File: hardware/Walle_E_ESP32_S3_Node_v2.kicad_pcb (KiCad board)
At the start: 2 copper layers, 160 x 100 mm, 50 parts, among them J1 Voltage01_ZMPT101B, J10 Conn_01x22_Pin, J11 Conn_01x22_Pin, J12 Conn_01x08_Pin, J13 Conn_01x08_Pin, J14 Diff_Pressure_Sens LWLP5000, J2 CurrentSens01_ACS712_5A, J4 CurrentSens03_ACS712_5A, J5 Conn_01x04_Pin, J6 +5VdcSupply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

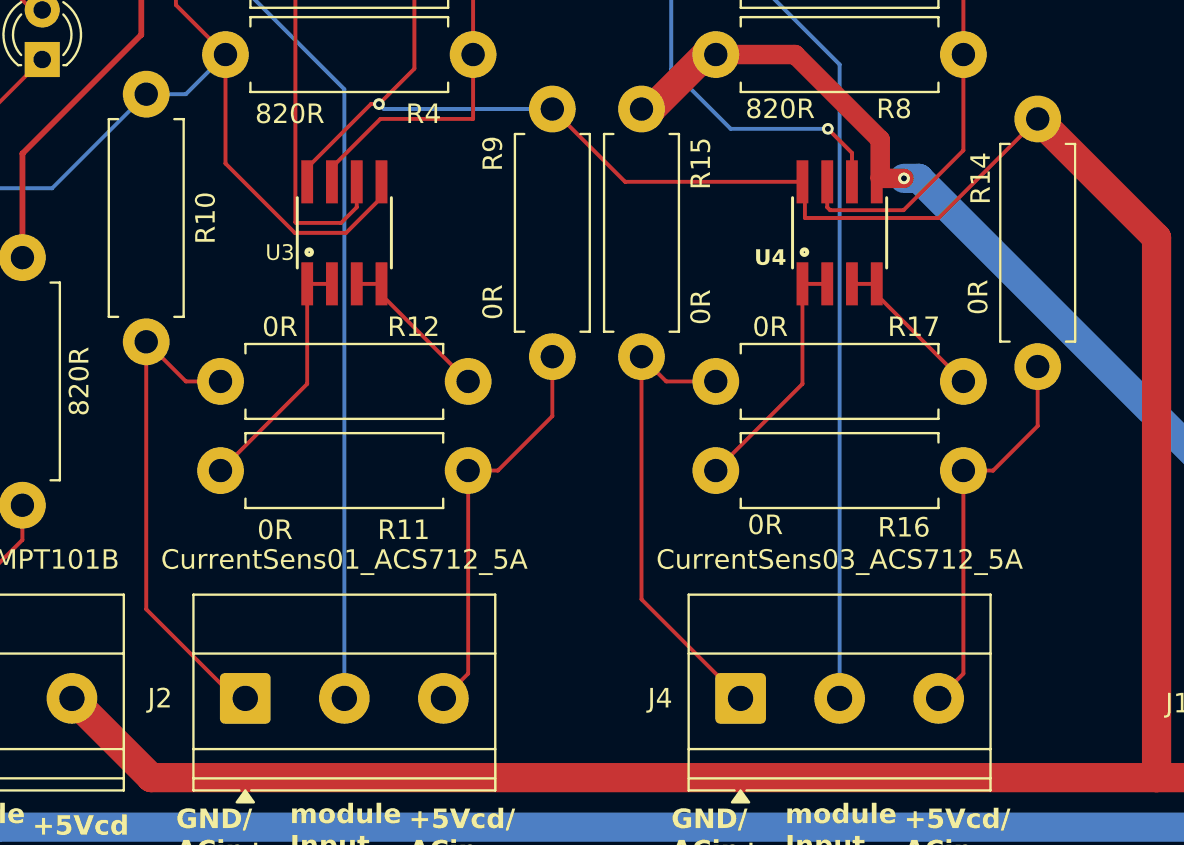
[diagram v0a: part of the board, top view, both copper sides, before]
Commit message: Thickness improve in AC current sensor input AC line
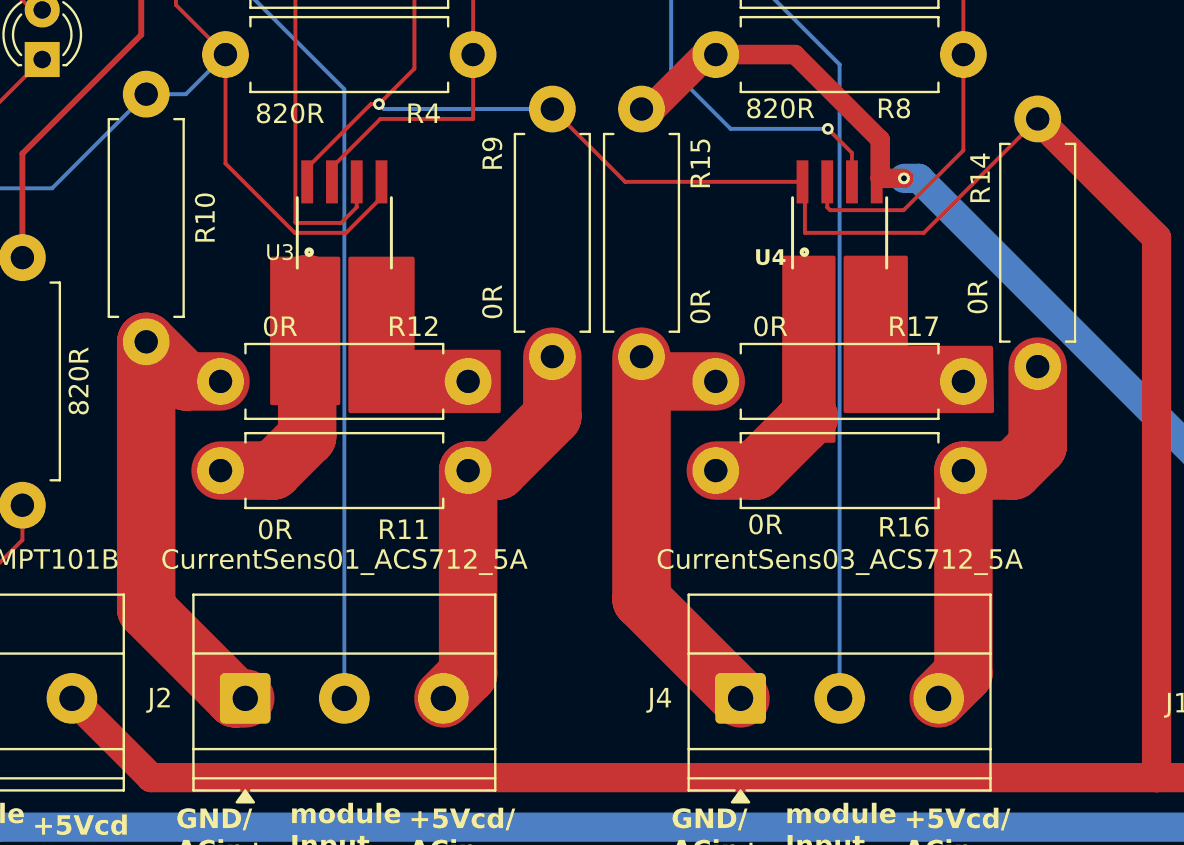
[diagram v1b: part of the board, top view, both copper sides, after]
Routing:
- net Net-(U4-IP-@3): track 8.11 -> 10.3 mm
- net Net-(U3-IP+@1): track 12.7 -> 14.3 mm
- net Net-(U4-IP+@1): track 12.7 -> 11.1 mm
- net +5V_input: track 330.8 -> 331.8 mm
- net Net-(U3-IP-@3): track 8.11 -> 9.14 mm
- net /CurrentSensor01_GND: track 26.1 -> 25.3 mm
- net /CurrentSensor03_+5V: track 20.0 -> 20.6 mm
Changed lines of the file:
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@@
 			(drillshape 0)
 			(scaleselection 1)
-			(outputdirectory "C:/Users/andani.lopez/KiCad projects/Wall_E_ESP32_Node/Wall_E_ESP32_Node_Gerber")
+			(outputdirectory "../Walle_E_ESP32_S3_Node_v2 Gerber/")
 		)
 	)
@@
 		)
 		(embedded_fonts no)
+		(model "${KIPRJMOD}/KiCad libraries/power supply/RAC05-0S5K_277_W/RAC05-05SK_277_W/RAC05-05SK_277_W.step"
+			(offset
+				(xyz 0 0 0)
+			)
+			(scale
+				(xyz 1 1 1)
+			)
+			(rotate
+				(xyz -90 -0 -0)
+			)
+		)
 	)
 	(footprint "TerminalBlock_Phoenix:TerminalBlock_Phoenix_MKDS-3-2-5.08_1x02_P5.08mm_Horizontal"
@@
 		)
 	)
+	(gr_poly
+		(pts
+			(xy 63.2968 68.834) (xy 63.2968 76.708) (xy 70.8152 76.708) (xy 70.7644 73.4568) (xy 66.3956 73.4568)
+			(xy 66.3956 68.834)
+		)
+		(stroke
+			(width 0.2)
+			(type solid)
+		)
+		(fill yes)
+		(layer "F.Cu")
+		(net 63)
+	)
+	(gr_poly
+		(pts
+			(xy 37.8968 68.8848) (xy 37.8968 76.708) (xy 45.5168 76.708) (xy 45.5168 73.66) (xy 41.0972 73.66)
+			(xy 41.0972 68.8848)
+		)
+		(stroke
+			(width 0.2)
+			(type solid)
+		)
+		(fill yes)
+		(layer "F.Cu")
+		(net 61)
+	)
+	(gr_poly
+		(pts
+			(xy 37.2872 76.3016) (xy 33.8836 76.3016) (xy 33.8836 68.8848) (xy 37.2872 68.8848)
+		)
+		(stroke
+			(width 0.2)
+			(type solid)
+		)
+		(fill yes)
+		(layer "F.Cu")
+		(net 60)
+	)
+	(gr_poly
+		(pts
+			(xy 60.1472 68.834) (xy 60.1472 78.232) (xy 62.6872 78.232) (xy 62.6872 68.834)
+		)
+		(stroke
+			(width 0.2)
+			(type solid)
+		)
+		(fill yes)
+		(layer "F.Cu")
+		(net 62)
+	)
 	(gr_rect
 		(start 0 0)
@@
 	)
 	(segment
+		(start 61.214 65.0748)
+		(end 61.214 67.564)
+		(width 0.2)
+		(layer "F.Cu")
+		(net 2)
+	)
+	(segment
 		(start 116.84 64.516)
 		(end 138.684 64.516)
@@
 	)
 	(segment
-		(start 61.087 64.9478)
-		(end 61.214 65.0748)
-		(width 0.2)
-		(layer "F.Cu")
-		(net 2)
-	)
-	(segment
 		(start 138.684 64.516)
 		(end 144.46 58.74)
@@
 	)
 	(segment
+		(start 67.31 67.564)
+		(end 73.152 61.722)
+		(width 0.2)
+		(layer "F.Cu")
+		(net 2)
+	)
+	(segment
 		(start 144.46 58.74)
 		(end 144.54 58.74)
@@
 	)
 	(segment
-		(start 41.185999 59.144001)
-		(end 39.37 60.96)
+		(start 61.087 64.9478)
+		(end 61.214 65.0748)
 		(width 0.2)
 		(layer "F.Cu")
@@
 	)
 	(segment
-		(start 38.954 60.96)
+		(start 41.185999 59.144001)
 		(end 39.37 60.96)
 		(width 0.2)
@@
 	)
 	(segment
-		(start 61.214 66.802)
-		(end 68.072 66.802)
+		(start 38.954 60.96)
+		(end 39.37 60.96)
 		(width 0.2)
 		(layer "F.Cu")
@@
 	)
 	(segment
-		(start 61.214 65.0748)
-		(end 61.214 66.802)
-		(width 0.2)
+		(start 27.686 95.504)
+		(end 23.876 91.694)
+		(width 1.5)
 		(layer "F.Cu")
 		(net 2)
 	)
 	(segment
-		(start 68.072 66.802)
-		(end 73.152 61.722)
+		(start 61.214 67.564)
+		(end 67.31 67.564)
 		(width 0.2)
 		(layer "F.Cu")
@@
 	)
 	(segment
-		(start 27.686 95.504)
-		(end 23.876 91.694)
-		(width 1.5)
-		(layer "F.Cu")
-		(net 2)
-	)
-	(segment
 		(start 35.687 64.9478)
 		(end 35.687 64.227)
@@
 	)
 	(segment
-		(start 32.512 91.44)
-		(end 32.512 91.948)
-		(width 0.2)
+		(start 27.432 86.868)
+		(end 27.432 73.152)
+		(width 3)
 		(layer "F.Cu")
 		(net 56)
 	)
 	(segment
-		(start 32.512 91.948)
+		(start 32.004 91.44)
 		(end 27.432 86.868)
-		(width 0.2)
+		(width 3)
+		(layer "F.Cu")
+		(net 56)
+	)
+	(segment
+		(start 32.512 91.44)
+		(end 32.004 91.44)
+		(width 3)
 		(layer "F.Cu")
 		(net 56)
@@
 		(start 29.464 75.184)
 		(end 27.432 73.152)
-		(width 0.2)
+		(width 3)
 		(layer "F.Cu")
 		(net 56)
@@
 		(start 31.242 75.184)
 		(end 29.464 75.184)
-		(width 0.2)
+		(width 3)
 		(layer "F.Cu")
 		(net 56)
 	)
 	(segment
-		(start 27.432 86.868)
-		(end 27.432 73.152)
-		(width 0.2)
+		(start 48.26 76.962)
+		(end 48.26 73.914)
+		(width 3)
 		(layer "F.Cu")
-		(net 56)
+		(net 57)
 	)
 	(segment
 		(start 45.466 79.756)
 		(end 48.26 76.962)
-		(width 0.2)
+		(width 3)
 		(layer "F.Cu")
 		(net 57)
 	)
 	(segment
-		(start 43.942 79.756)
-		(end 45.466 79.756)
-		(width 0.2)
+		(start 42.672 91.44)
+		(end 43.942 90.17)
+		(width 3)
 		(layer "F.Cu")
 		(net 57)
 	)
 	(segment
-		(start 48.26 76.962)
-		(end 48.26 73.914)
-		(width 0.2)
+		(start 43.942 90.17)
+		(end 43.942 79.756)
+		(width 3)
 		(layer "F.Cu")
 		(net 57)
 	)
 	(segment
-		(start 42.672 91.44)
-		(end 43.942 90.17)
-		(width 0.2)
+		(start 43.942 79.756)
+		(end 45.466 79.756)
+		(width 3)
 		(layer "F.Cu")
 		(net 57)
 	)
 	(segment
-		(start 43.942 90.17)
-		(end 43.942 79.756)
-		(width 0.2)
+		(start 71.882 79.756)
+		(end 73.152 78.486)
+		(width 3)
 		(layer "F.Cu")
-		(net 57)
+		(net 58)
 	)
 	(segment
 		(start 69.342 79.756)
-		(end 70.866 79.756)
-		(width 0.2)
+		(end 71.882 79.756)
+		(width 3)
 		(layer "F.Cu")
 		(net 58)
@@
 		(start 69.342 90.17)
 		(end 69.342 79.756)
-		(width 0.2)
-		(layer "F.Cu")
-		(net 58)
-	)
-	(segment
-		(start 70.866 79.756)
-		(end 73.152 77.47)
-		(width 0.2)
+		(width 3)
 		(layer "F.Cu")
 		(net 58)
@@
 		(start 68.072 91.44)
 		(end 69.342 90.17)
-		(width 0.2)
+		(width 3)
 		(layer "F.Cu")
 		(net 58)
 	)
 	(segment
-		(start 73.152 77.47)
+		(start 73.152 78.486)
 		(end 73.152 74.422)
-		(width 0.2)
+		(width 3)
 		(layer "F.Cu")
 		(net 58)
@@
 		(start 54.102 75.184)
 		(end 56.642 75.184)
-		(width 0.2)
+		(width 3)
 		(layer "F.Cu")
 		(net 59)
@@
 		(start 57.912 91.44)
 		(end 52.832 86.36)
-		(width 0.2)
+		(width 3)
 		(layer "F.Cu")
 		(net 59)
@@
 		(start 52.832 86.36)
 		(end 52.832 73.914)
-		(width 0.2)
+		(width 3)
 		(layer "F.Cu")
 		(net 59)
 	)
 	(segment
+		(start 33.9344 79.756)
+		(end 31.242 79.756)
+		(width 3)
+		(layer "F.Cu")
+		(net 60)
+	)
+	(segment
 		(start 35.687 70.1802)
-		(end 36.957 70.1802)
-		(width 0.2)
+		(end 35.687 78.0034)
+		(width 3)
 		(layer "F.Cu")
 		(net 60)
@@
 	(segment
 		(start 35.687 70.1802)
-		(end 35.687 75.311)
+		(end 36.957 70.1802)
 		(width 0.2)
 		(layer "F.Cu")
@@
 	)
 	(segment
-		(start 35.687 75.311)
-		(end 31.242 79.756)
-		(width 0.2)
+		(start 35.687 78.0034)
+		(end 33.9344 79.756)
+		(width 3)
 		(layer "F.Cu")
 		(net 60)
 	)
 	(segment
+		(start 39.497 74.6506)
+		(end 40.0304 75.184)
+		(width 3)
+		(layer "F.Cu")
+		(net 61)
+	)
+	(segment
 		(start 39.497 70.1802)
 		(end 39.497 70.739)
@@
 	(segment
 		(start 39.497 70.739)
-		(end 43.942 75.184)
-		(width 0.2)
+		(end 39.497 74.6506)
+		(width 3)
 		(layer "F.Cu")
 		(net 61)
 	)
 	(segment
-		(start 39.497 70.1802)
-		(end 38.227 70.1802)
-		(width 0.2)
+		(start 40.0304 75.184)
+		(end 43.942 75.184)
+		(width 3)
 		(layer "F.Cu")
 		(net 61)
 	)
 	(segment
-		(start 56.642 79.756)
-		(end 61.087 75.311)
-		(width 0.2)
+		(start 61.4172 77.0128)
+		(end 61.4172 73.533)
+		(width 2.7)
 		(layer "F.Cu")
 		(net 62)
@@
 	)
 	(segment
-		(start 61.087 75.311)
-		(end 61.087 70.1802)
-		(width 0.2)
+		(start 56.642 79.756)
+		(end 58.674 79.756)
+		(width 3)
+		(layer "F.Cu")
+		(net 62)
+	)
+	(segment
+		(start 61.4172 77.0128)
+		(end 61.087 77.343)
+		(width 3)
+		(layer "F.Cu")
+		(net 62)
+	)
+	(segment
+		(start 58.674 79.756)
+		(end 61.4172 77.0128)
+		(width 3)
 		(layer "F.Cu")
 		(net 62)
 	)
 	(segment
+		(start 64.897 70.1802)
+		(end 64.897 70.739)
+		(width 0.2)
+		(layer "F.Cu")
+		(net 63)
+	)
+	(segment
+		(start 64.897 74.549)
+		(end 65.532 75.184)
+		(width 3)
+		(layer "F.Cu")
+		(net 63)
+	)
+	(segment
 		(start 63.627 70.1802)
 		(end 64.897 70.1802)
@@
 	)
 	(segment
-		(start 64.897 70.1802)
-		(end 64.897 70.739)
-		(width 0.2)
+		(start 65.532 75.184)
+		(end 69.342 75.184)
+		(width 3)
 		(layer "F.Cu")
 		(net 63)
@@
 	(segment
 		(start 64.897 70.739)
-		(end 69.342 75.184)
-		(width 0.2)
+		(end 64.897 74.549)
+		(width 3)
 		(layer "F.Cu")
 		(net 63)

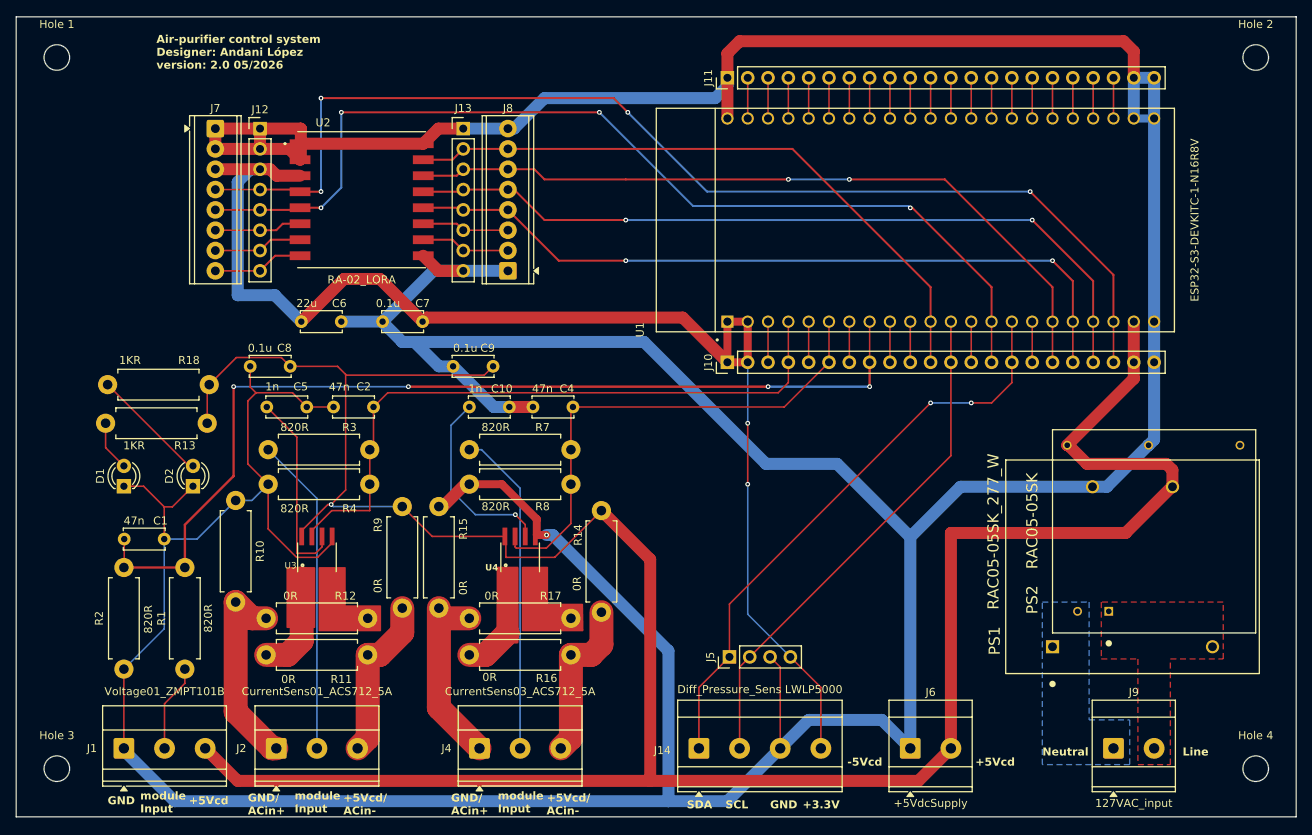
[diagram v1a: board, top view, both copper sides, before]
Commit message: AC line corrections: trace width, routing improvements and Gerber update
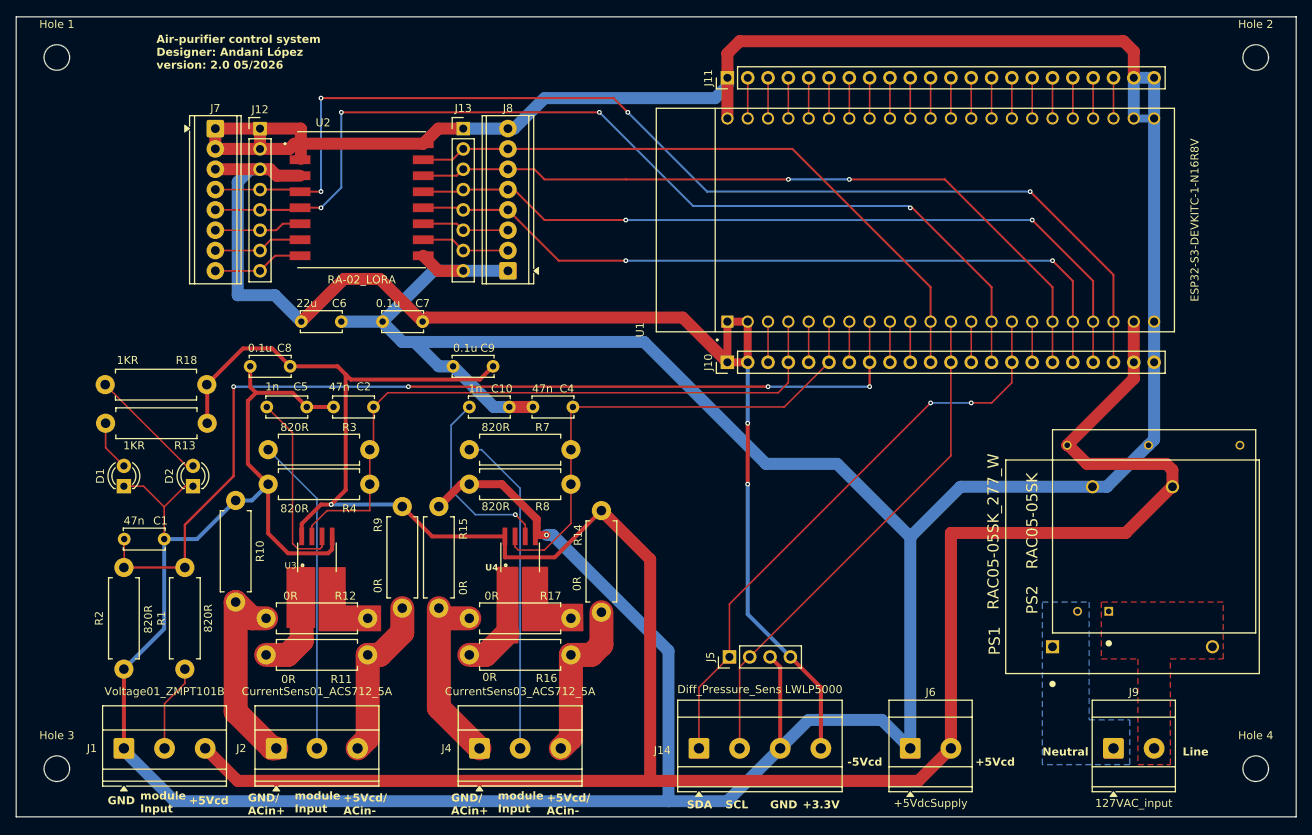
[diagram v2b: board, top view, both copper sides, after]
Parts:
- moved R18 0.30 mm to (23.8, 46.0)
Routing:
- net +5V_input: track 331.8 -> 334.0 mm
- net GND: track 675.2 -> 676.8 mm
- net Net-(U3-FILT): track 24.6 -> 23.8 mm
